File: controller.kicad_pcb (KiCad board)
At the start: 2 copper layers, 60 x 122 mm, 150 parts, among them J1 KYCON_KPJX-4S-S, J10 MicroFit_2x04, J11 JST_S4B-XH, J12 MicroFit_2x04, J13 JST_B2B-XH, J14 JST_S2B-XH, J16 MLX_1x03, J17 MLX_1x03, J2 MicroFit_2x02, J3 24V/5A OUT, J4 DB25 FEMALE, J5 JST_S6B-XH, J6 JST_S4B-XH, J7 MicroFit_2x04, J8 JST_S4B-XH, J9 JST_S4B-XH, K1 OJS-SH-124HMF, Q1 BC847, Q2 IRF9540SPBF, Q3 BC857, Q4 BC847, Q5 BC857, U1 MC78M12CDT-TR, U2 MAX5035BUSA, U3 LM358EDR2G, U4 74HC245, U5 74HC245, U6 ACSL-6310, U7 ACSL-6310

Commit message: Changed name to Shapeoko LPT Interface v2.0
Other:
- board text added: "Shapeoko LPT Interface v2.0"
- board text removed: "Shapeoko UCCNC Controller Interface v2.0"
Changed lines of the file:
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@@
   (paper "A4")
   (title_block
-    (title "Shapeoko UCCNC Controller Interface")
-    (date "2022-05-24")
+    (title "Shapeoko LPT Interface")
+    (date "2022-06-02")
     (rev "2.0")
     (company "Gruvin & Co")
@@
     (effects (font (size 1 1) (thickness 0.15)) (justify right mirror))
   )
+  (gr_text "AGND" (at 131.45 95.2) (layer "B.SilkS")
+    (effects (font (size 1 1) (thickness 0.15)) (justify left mirror))
+  )
   (gr_text "YCLK" (at 131.7 120.375) (layer "B.SilkS")
     (effects (font (size 1 1) (thickness 0.15)) (justify left mirror))
@@
     (effects (font (size 1 1) (thickness 0.15)) (justify left mirror))
   )
-  (gr_text "AGND" (at 131.45 95.2) (layer "B.SilkS")
-    (effects (font (size 1 1) (thickness 0.15)) (justify left mirror))
-  )
   (gr_text "P17" (at 87.85 85.375) (layer "B.SilkS")
     (effects (font (size 1 1) (thickness 0.15)) (justify left mirror))
@@
     (effects (font (size 0.6 0.6) (thickness 0.13)) (justify right mirror))
   )
-  (gr_text "Shapeoko UCCNC Controller Interface v2.0" (at 105.3 84.8 90) (layer "B.SilkS")
+  (gr_text "Shapeoko LPT Interface v2.0" (at 105.3 84.8 90) (layer "B.SilkS")
     (effects (font (size 1.5 1.5) (thickness 0.3)) (justify left mirror))
   )
@@
     (effects (font (size 0.8 0.7) (thickness 0.125)))
   )
-  (gr_text "RL3" (at 128.85 155.4 90) (layer "F.SilkS")
-    (effects (font (size 0.5 0.5) (thickness 0.08)))
-  )
   (gr_text "BitSetter" (at 104.4 162.35) (layer "F.SilkS")
     (effects (font (size 0.8 0.7) (thickness 0.125)))
@@
     (effects (font (size 0.7 0.7) (thickness 0.1)))
   )
-  (gr_text "RL4*" (at 128.85 157.9 90) (layer "F.SilkS")
+  (gr_text "RL3" (at 128.85 155.4 90) (layer "F.SilkS")
     (effects (font (size 0.5 0.5) (thickness 0.08)))
   )
@@
     (effects (font (size 1 1) (thickness 0.125)))
   )
+  (gr_text "RL4*" (at 128.85 157.9 90) (layer "F.SilkS")
+    (effects (font (size 0.5 0.5) (thickness 0.08)))
+  )
   (gr_text "CLK" (at 128.85 135.4 90) (layer "F.SilkS")
     (effects (font (size 0.5 0.5) (thickness 0.08)))
@@
   (via (at 120.6 50.25) (size 1) (drill 0.6) (layers "F.Cu" "B.Cu") (net 4))
   (via (at 107.8 55.05) (size 0.7) (drill 0.3) (layers "F.Cu" "B.Cu") (net 4))
-  (via (at 125.4 69.45) (size 1) (drill 0.6) (layers "F.Cu" "B.Cu") (net 4))
   (via (at 125.4 50.25) (size 1) (drill 0.6) (layers "F.Cu" "B.Cu") (net 4))
   (via (at 119 56.65) (size 1) (drill 0.6) (layers "F.Cu" "B.Cu") (net 4))
@@
   (via (at 112.6 51.85) (size 0.7) (drill 0.3) (layers "F.Cu" "B.Cu") (net 4))
   (via (at 120.6 66.25) (size 1) (drill 0.6) (layers "F.Cu" "B.Cu") (net 4))
+  (via (at 125.4 69.45) (size 1) (drill 0.6) (layers "F.Cu" "B.Cu") (net 4))
   (via (at 127 72.65) (size 1) (drill 0.6) (layers "F.Cu" "B.Cu") (net 4))
   (via (at 120.6 59.85) (size 1) (drill 0.6) (layers "F.Cu" "B.Cu") (net 4))

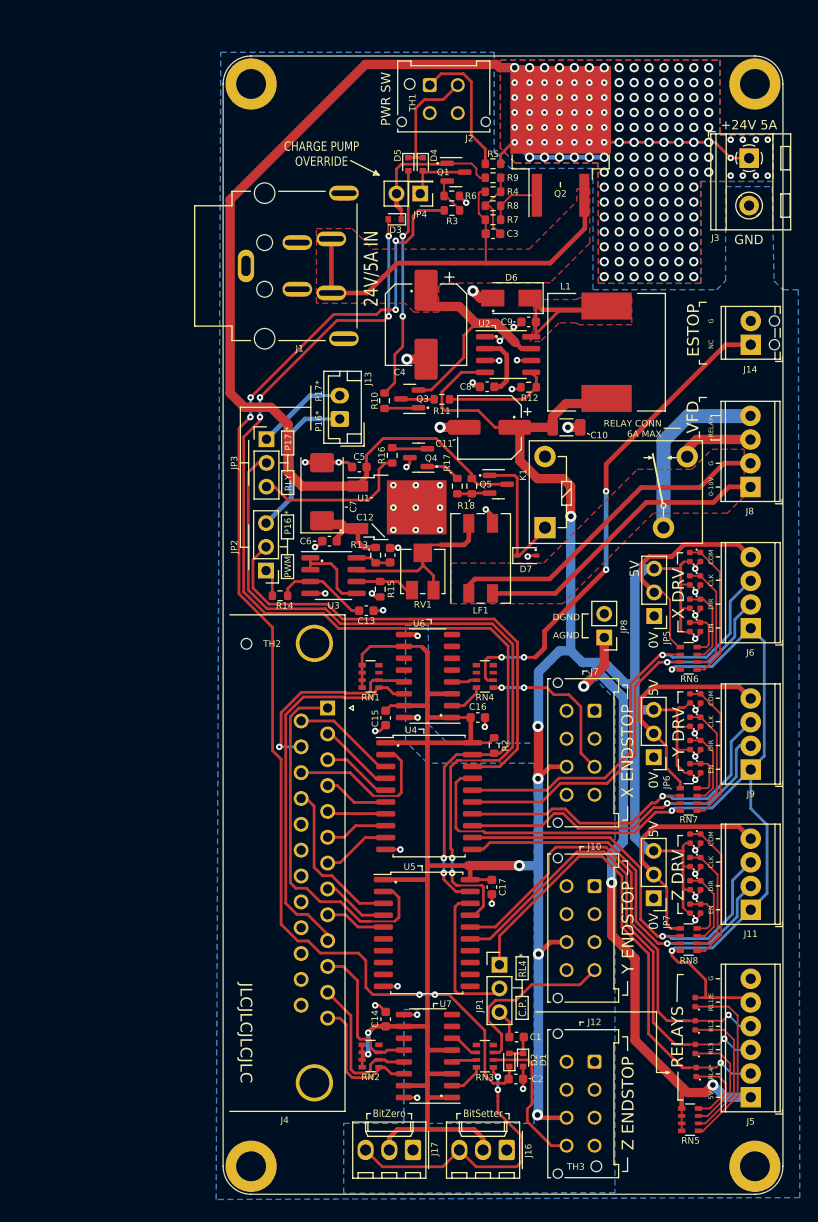
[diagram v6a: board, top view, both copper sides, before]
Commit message: 'Fixed' CAM/Grid origins.
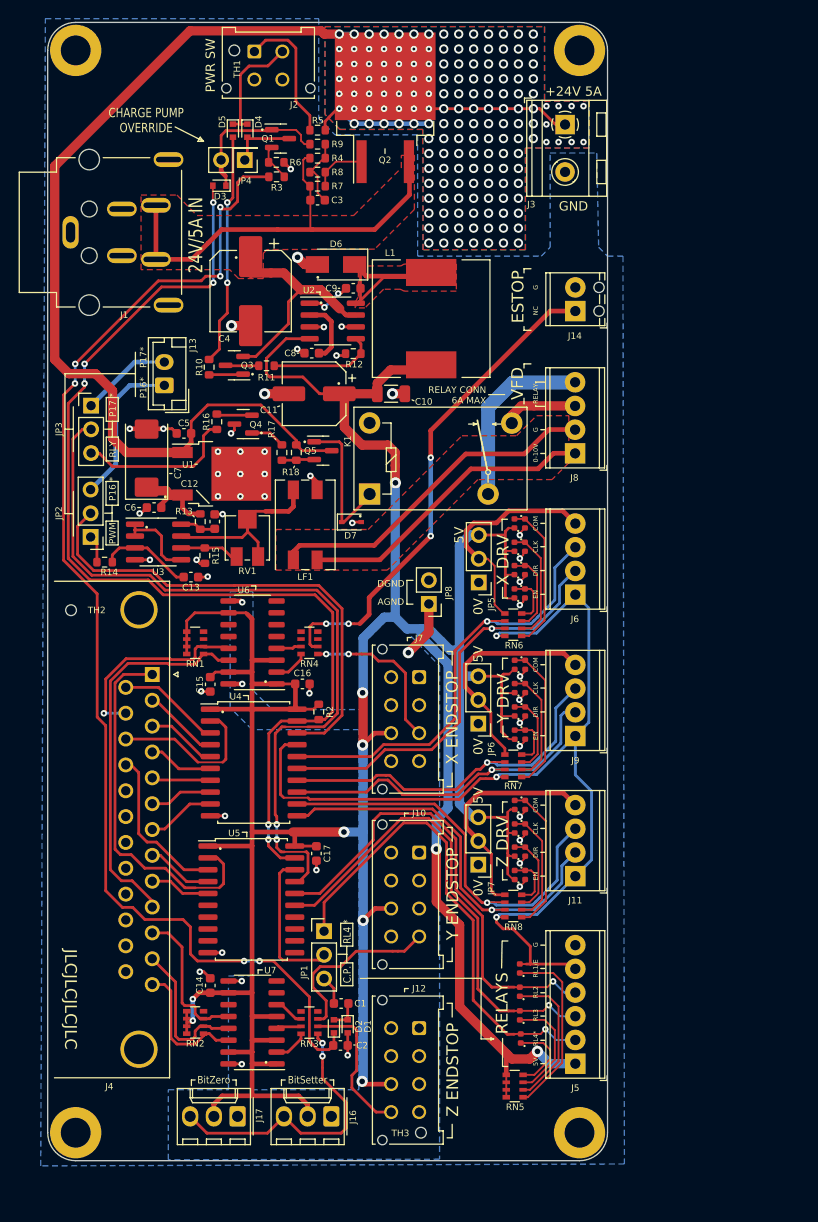
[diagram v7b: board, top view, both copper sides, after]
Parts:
- moved J3 20.1 mm to (113.2, 56.4)
- moved D9 19.1 mm to (108.3, 151.8)
- moved NT11 19.1 mm to (90.8, 153.7)
- moved NT18 19.1 mm to (110.2, 139.4)
- moved C13 19.1 mm to (73.1, 104.8)
- moved C5 19.1 mm to (72.3, 89.5)
- moved C7 19.1 mm to (68.3, 92.1)
- moved D10 19.1 mm to (108.3, 149.3)
- moved D11 19.1 mm to (108.3, 146.8)
- moved D5 19.1 mm to (77.6, 57.0)
- moved H2 19.1 mm to (114.8, 48.4)
- moved H4 19.1 mm to (114.8, 164.4)
- moved J1 19.1 mm to (69.3, 67.9)
- moved J17 19.1 mm to (78.1, 162.7)
- moved JP8 19.1 mm to (98.6, 107.7)
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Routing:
- net 24V_SAFE: track 135.1 -> 134.2 mm
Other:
- board text added: "+24V IN"
- board text added: "ES"
- board text added: "NO"
- board text removed: "!ES!"
- board text removed: "+24V"

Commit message: Silkscreen errors
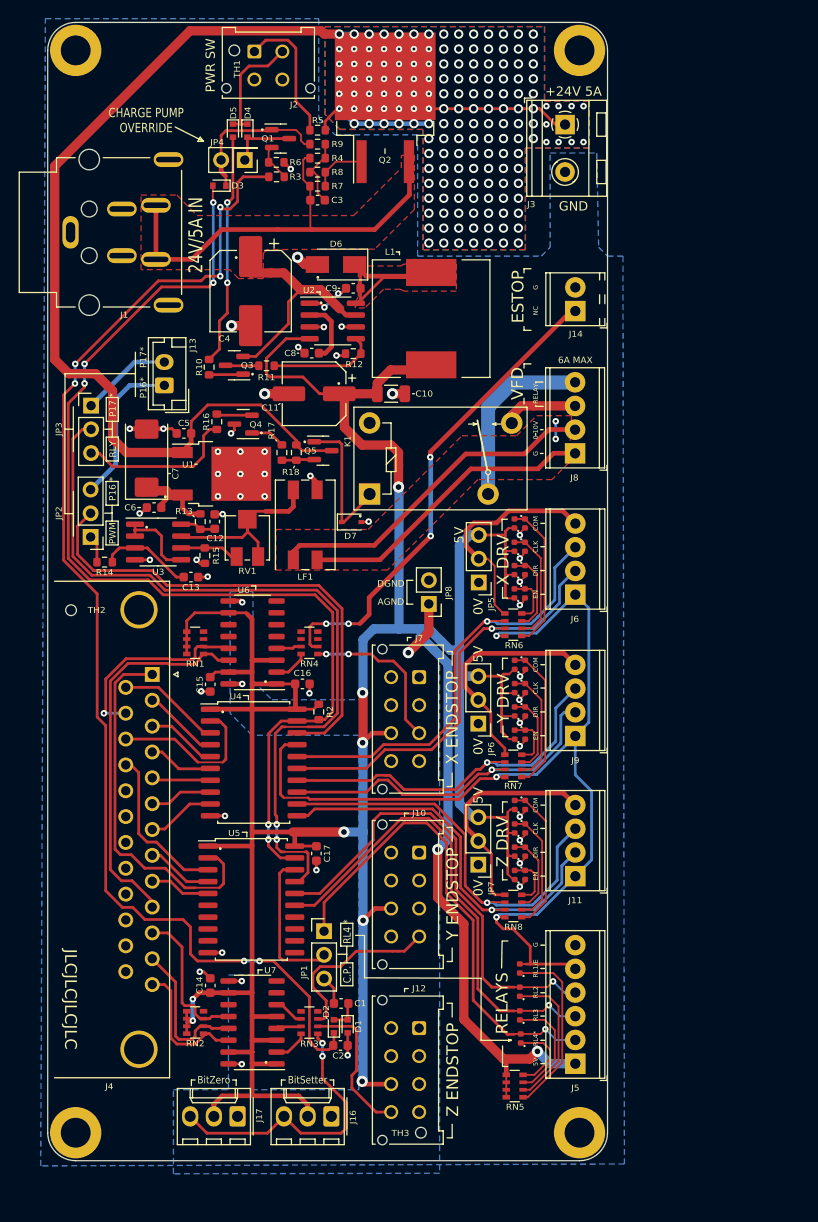
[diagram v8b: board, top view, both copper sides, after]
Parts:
- J14: footprint TerminalBlock_Phoenix:TerminalBlock_Phoenix_MPT-0,5-2-2.54_1x02_P2.54mm_Horizontal -> -Project:TerminalBlock_Phoenix_MPT-0,5-2-2.54_1x02_P2.54mm_Horizontal
- moved NT3 0.35 mm to (95.3, 92.2)
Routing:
- net /Connectors/VFD_AGND: track 32.4 -> 34.3 mm, vias 0 -> 2
- net /Connectors/EMRG_STOP: track 44.7 -> 43.4 mm
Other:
- board text added: "0 10V"
- board text added: "6A MAX"
- board text removed: "0-10V"
- board text removed: "RELAY CONN 6A MAX"
